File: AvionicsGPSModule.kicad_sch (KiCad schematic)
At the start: 33 parts, among them P1 MC311D, Q1 AO3400A, U1 RP2040, U2 AP2112K-3.3, U3 L80-R, U4 W25Q128JVS, X1 ABM8-272-T3

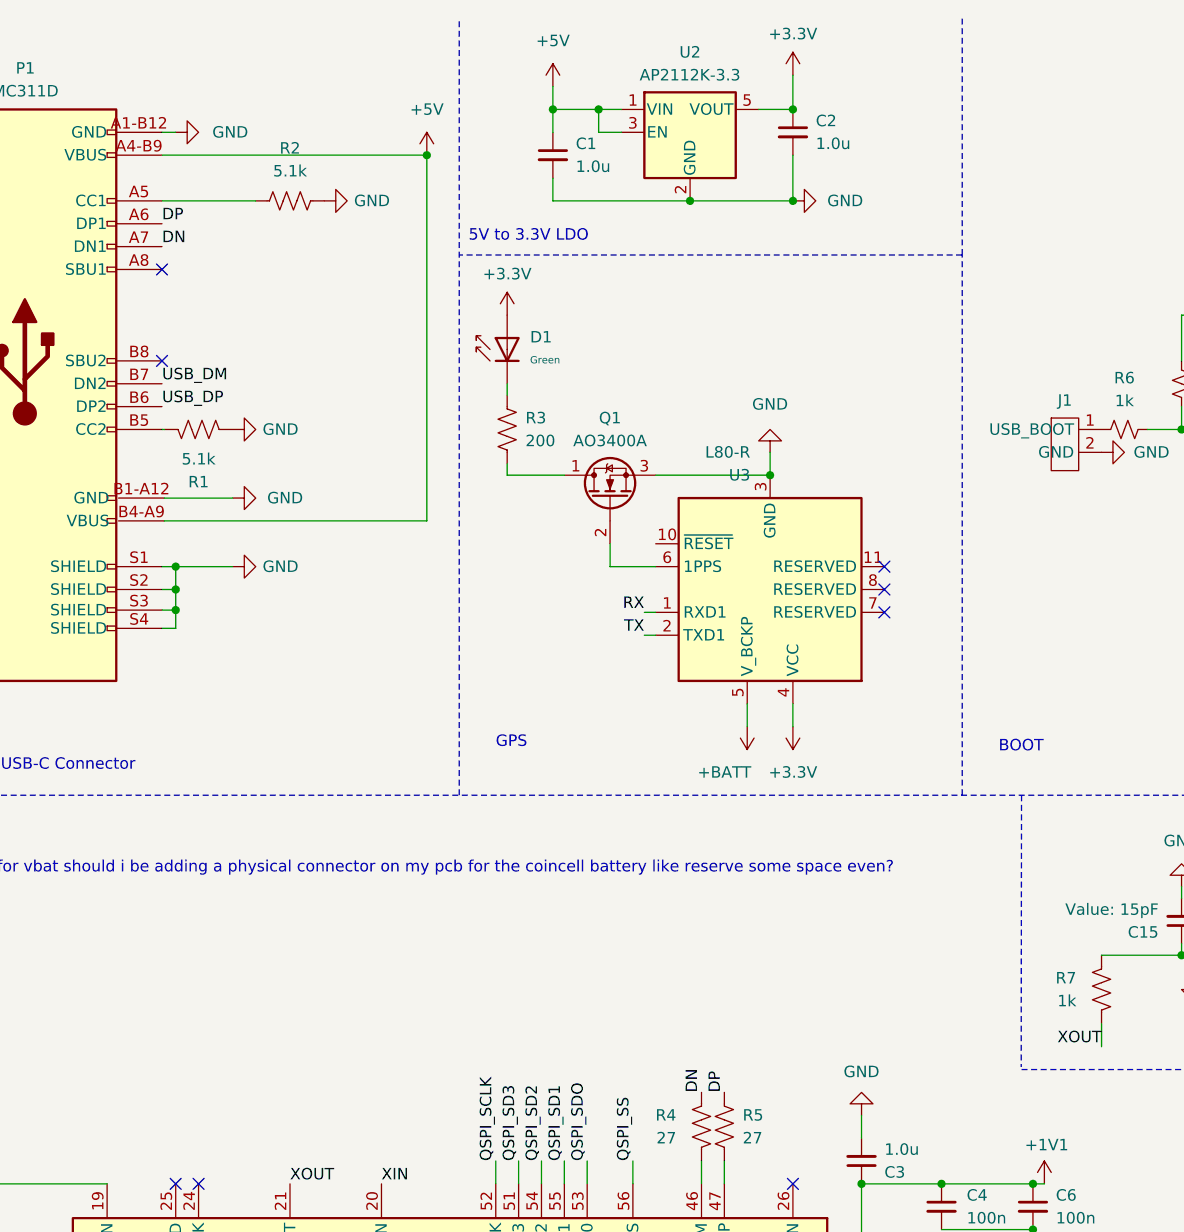
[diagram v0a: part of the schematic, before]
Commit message: Fixed Differential Pair Wiring
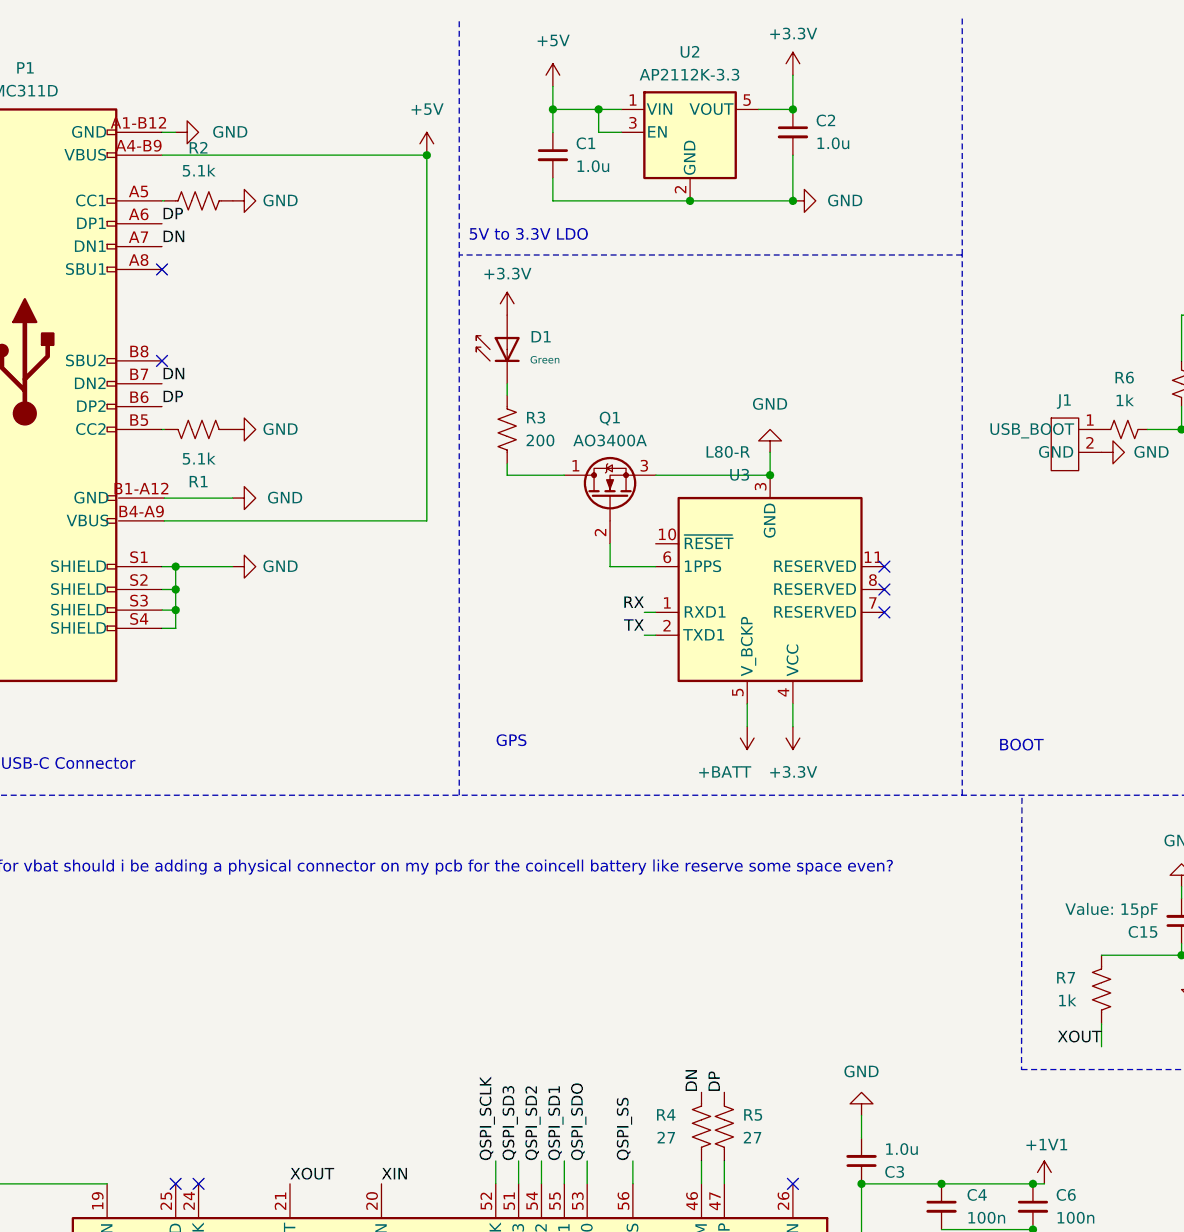
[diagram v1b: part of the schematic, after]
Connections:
- net USB_DM is gone; now on net DN: P1.B7 (DN2)
- net USB_DP is gone; now on net DP: P1.B6 (DP2)
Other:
- moved on the sheet: R2
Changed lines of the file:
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@@
 	(polyline
 		(pts
-			(xy 134.62 99.06) (xy 134.578 129.2512)
+			(xy 134.662 99.3488) (xy 134.62 129.54)
 		)
 		(stroke
@@
 	(wire
 		(pts
-			(xy 39.116 33.02) (xy 49.53 33.02)
+			(xy 39.116 33.02) (xy 39.37 33.02)
 		)
 		(stroke
@@
 		)
 	)
+	(label "DN"
+		(at 39.116 53.34 0)
+		(effects
+			(font
+				(size 1.27 1.27)
+			)
+			(justify left bottom)
+		)
+	)
 	(label "TX"
 		(at 109.22 193.04 270)
@@
 		)
 	)
-	(label "RX"
-		(at 106.68 193.04 270)
+	(label "DP"
+		(at 39.116 55.88 0)
 		(effects
 			(font
 				(size 1.27 1.27)
 			)
-			(justify right bottom)
+			(justify left bottom)
 		)
 	)
 	(label "RX"
-		(at 92.71 78.74 180)
+		(at 106.68 193.04 270)
 		(effects
 			(font
@@
 		)
 	)
-	(label "QSPI_SS"
-		(at 167.64 58.42 180)
+	(label "RX"
+		(at 92.71 78.74 180)
 		(effects
 			(font
@@
 		)
 	)
-	(label "USB_DP"
-		(at 39.116 55.88 0)
+	(label "QSPI_SS"
+		(at 167.64 58.42 180)
 		(effects
 			(font
 				(size 1.27 1.27)
 			)
-			(justify left bottom)
+			(justify right bottom)
 		)
 	)
@@
 		)
 	)
-	(label "USB_DM"
-		(at 39.116 53.34 0)
-		(effects
-			(font
-				(size 1.27 1.27)
-			)
-			(justify left bottom)
-		)
-	)
 	(label "QSPI_SD2"
 		(at 81.28 139.7 90)
@@
 	(symbol
 		(lib_id "Device:R_US")
-		(at 53.34 33.02 90)
+		(at 43.18 33.02 90)
 		(unit 1)
 		(exclude_from_sim no)
@@
 		(fields_autoplaced yes)
 		(property "Reference" "R2"
-			(at 53.34 27.178 90)
+			(at 43.18 27.178 90)
 			(effects
 				(font
@@
 		)
 		(property "Value" "5.1k"
-			(at 53.34 29.718 90)
+			(at 43.18 29.718 90)
 			(effects
 				(font
@@
 		)
 		(property "Footprint" "Resistor_SMD:R_0402_1005Metric"
-			(at 53.594 32.004 90)
+			(at 43.434 32.004 90)
 			(effects
 				(font
@@
 		)
 		(property "Datasheet" "~"
-			(at 53.34 33.02 0)
+			(at 43.18 33.02 0)
 			(effects
 				(font
@@
 		)
 		(property "Description" ""
-			(at 53.34 33.02 0)
+			(at 43.18 33.02 0)
 			(effects
 				(font
@@
 		)
 		(property "LCSC" "C25905"
-			(at 53.34 33.02 0)
+			(at 43.18 33.02 0)
 			(effects
 				(font
@@
 	(symbol
 		(lib_id "power:GND")
-		(at 57.15 33.02 90)
+		(at 46.99 33.02 90)
 		(unit 1)
 		(exclude_from_sim no)
@@
 		(fields_autoplaced yes)
 		(property "Reference" "#PWR06"
-			(at 63.5 33.02 0)
+			(at 53.34 33.02 0)
 			(effects
 				(font
@@
 		)
 		(property "Value" "GND"
-			(at 60.452 33.02 90)
+			(at 50.292 33.02 90)
 			(effects
 				(font
@@
 		)
 		(property "Footprint" ""
-			(at 57.15 33.02 0)
+			(at 46.99 33.02 0)
 			(effects
 				(font
@@
 		)
 		(property "Datasheet" ""
-			(at 57.15 33.02 0)
+			(at 46.99 33.02 0)
 			(effects
 				(font
@@
 		)
 		(property "Description" ""
-			(at 57.15 33.02 0)
+			(at 46.99 33.02 0)
 			(effects
 				(font

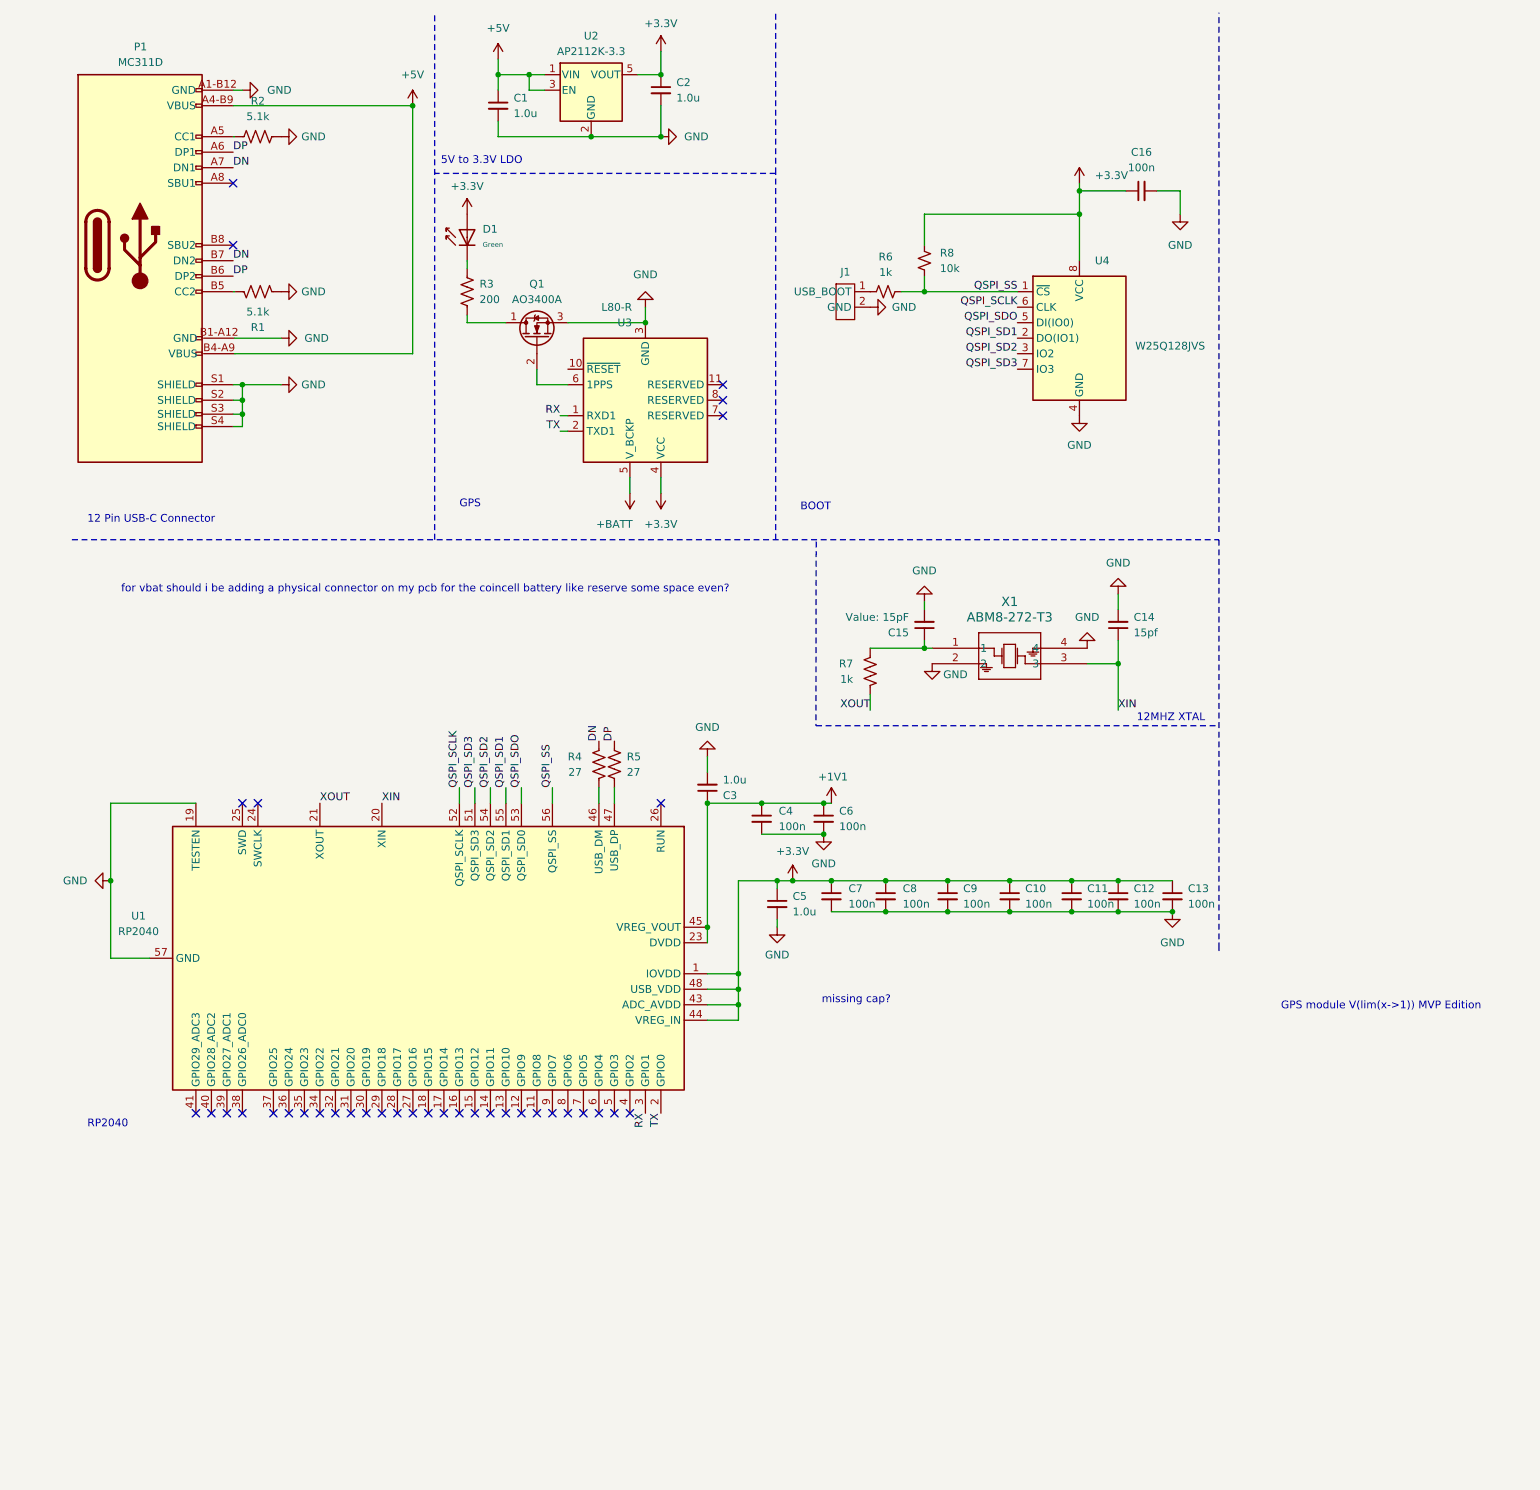
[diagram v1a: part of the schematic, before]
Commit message: Added mounting holes and LEDs, changed outline
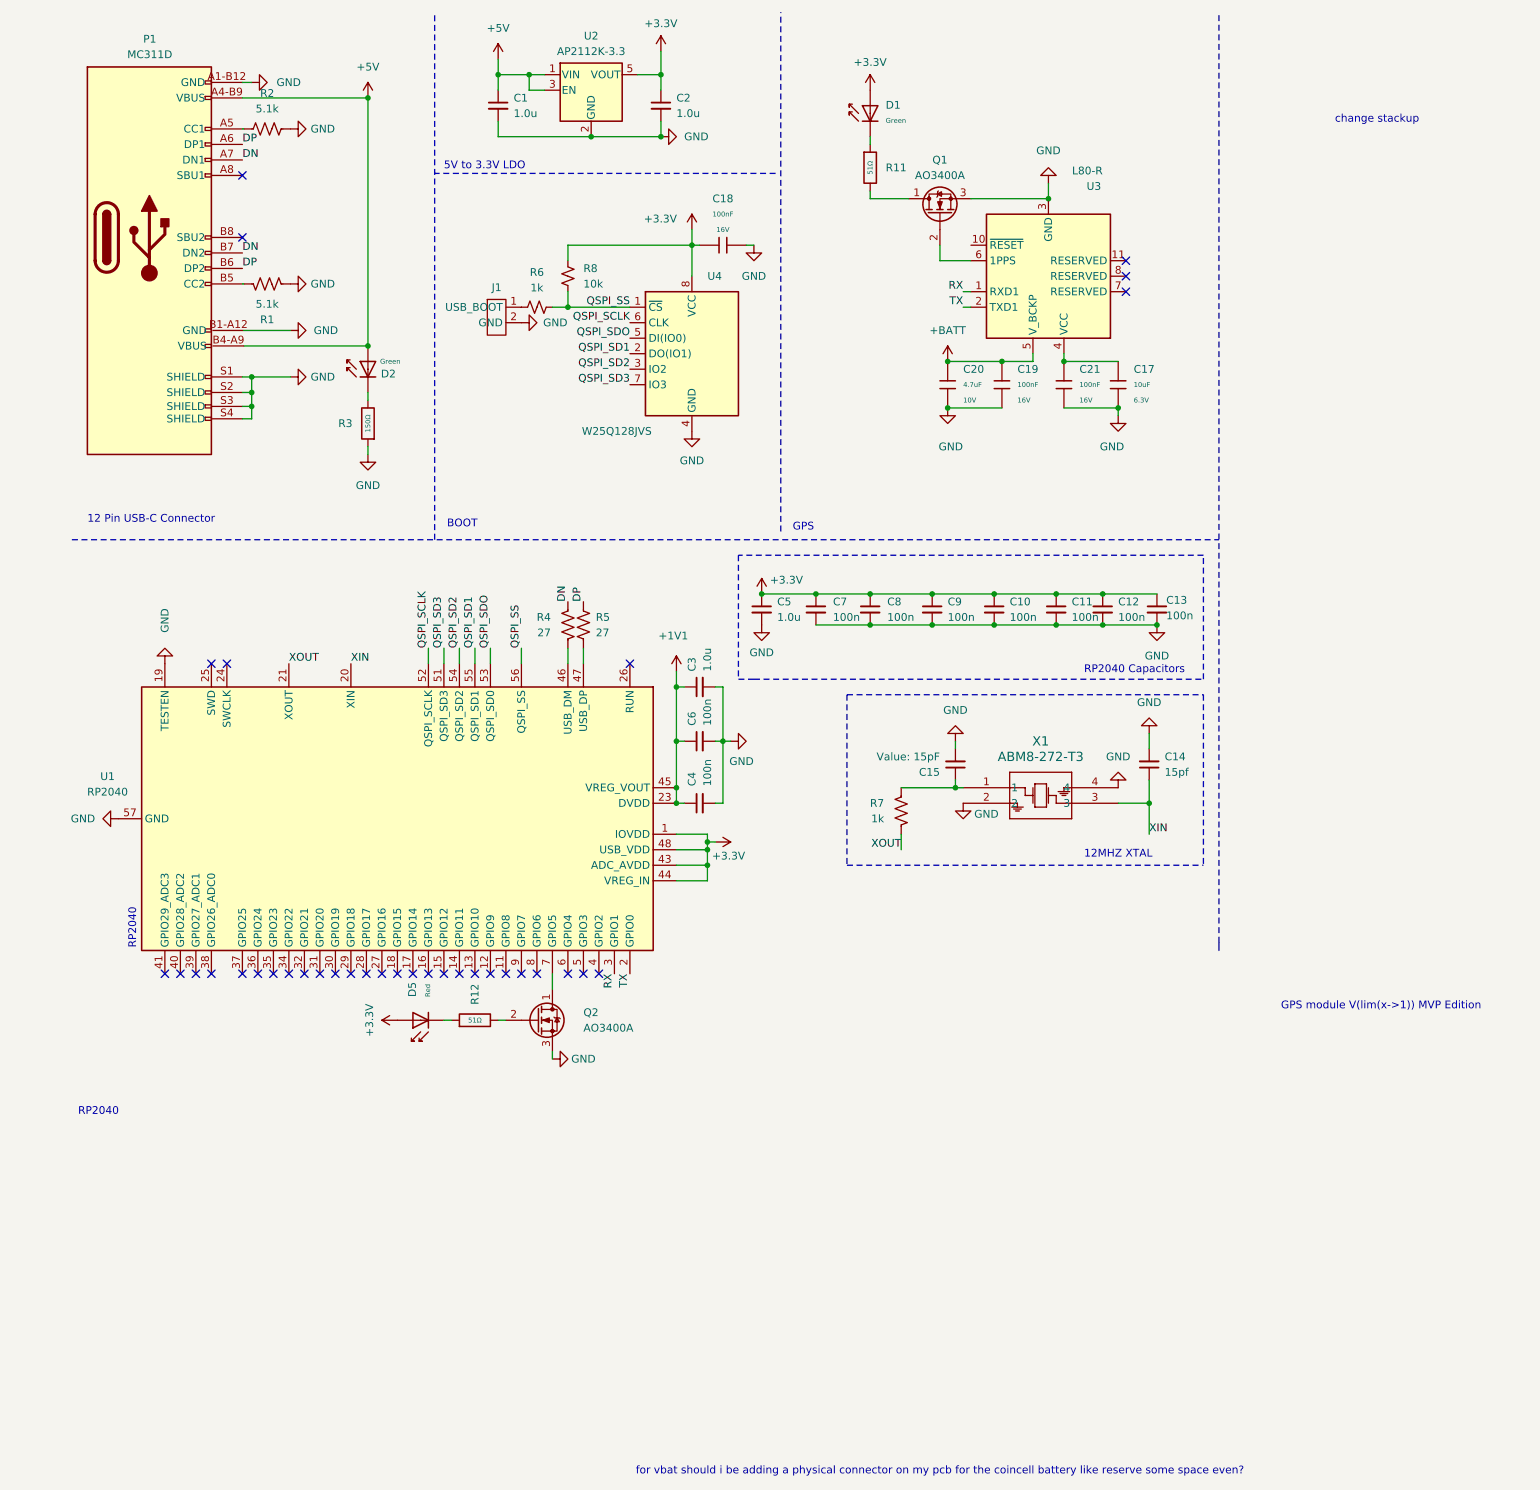
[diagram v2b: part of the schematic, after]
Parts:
- removed C16: 100n, Capacitor_SMD:C_0402_1005Metric, symbol Device:C_Small
- removed R3: 200, Resistor_SMD:R_0402_1005Metric, symbol Device:R_US
- added C17: 10uF, PCM_JLCPCB:C_0402, symbol PCM_JLCPCB-Capacitors:0402,10uF
- added C18, C19, C21: 100nF, PCM_JLCPCB:C_0402, symbol PCM_JLCPCB-Capacitors:0402,100nF
- added C20: 4.7uF, PCM_JLCPCB:C_0402, symbol PCM_JLCPCB-Capacitors:0402,4.7uF
- added D2: Green, PCM_JLCPCB:D_0805, symbol PCM_JLCPCB-Diodes:LED,0805,Green
- added D5: Red, PCM_JLCPCB:D_0805, symbol PCM_JLCPCB-Diodes:LED,0805,Red
- added Q2: AO3400A, AO3400A:SOT-23-3L_AOS, symbol Device:Q_NMOS_DGS
- added R11, R12: 51Ω, PCM_JLCPCB:R_0402, symbol PCM_JLCPCB-Resistors:0402,51Ω
- added R3: 150Ω, PCM_JLCPCB:R_0402, symbol PCM_JLCPCB-Resistors:0402,150Ω
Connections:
- net +3.3V: now also C18.1, D5.2; no longer U3.4 (VCC)
- net +5V: now also D2.2
- net +BATT: now also C19.1, C20.1
- net GND: now also C17.2, C18.2, C19.2, C20.2, C21.2, Q2.3 (S), R3.1
- net at Q1.1 (D): now also R11.2
- net at U1.7 (GPIO5): now also Q2.1 (D)
- net at D1.1: now also R11.1
- new net: Q2.2 (G), R12.2
- new net: D5.1, R12.1
- new net: C17.1, C21.1, U3.4 (VCC)
- new net: D2.1, R3.2
- no-connect marks 36 -> 35
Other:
- note added: "RP2040 Capacitors"
- note added: "change stackup"
- note removed: "missing cap?"
- moved on the sheet: C10, C11, C12, C13, C14, C15, C2, C3, C4, C5, C6, C7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
